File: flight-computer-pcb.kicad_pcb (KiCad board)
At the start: 4 copper layers, 140 x 80 mm, 3 parts, among them U1 Teensy4.1, U2 BMP390, U3 BNO055

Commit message: feat: add GND layer
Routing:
- added copper zone on In1.Cu, net GND
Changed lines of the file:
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@@
 		(layer "Edge.Cuts")
+	)
+	(zone
+		(net 4)
+		(net_name "GND")
+		(layer "In1.Cu")
+		(hatch edge 0.5)
+		(connect_pads
+			(clearance 0.5)
+		)
+		(min_thickness 0.25)
+		(filled_areas_thickness no)
+		(fill yes
+			(thermal_gap 0.5)
+			(thermal_bridge_width 0.5)
+		)
+		(polygon
+			(pts
+				(xy 71.177899 56) (xy 229.177899 56) (xy 229.177899 146) (xy 70.177899 146)
+			)
+		)
 	)
 	(embedded_fonts no)

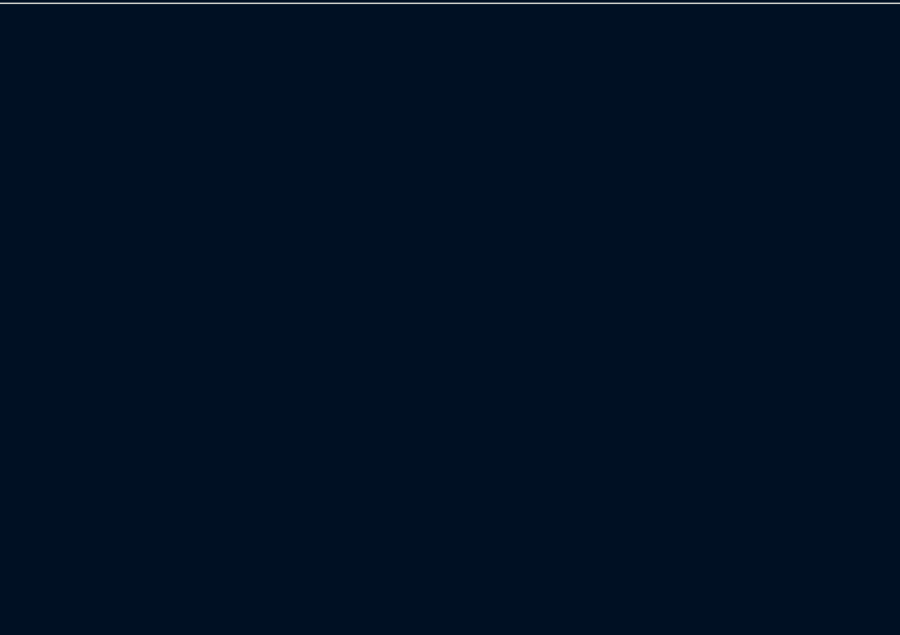
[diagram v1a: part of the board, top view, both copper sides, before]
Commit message: feat: add S13V10F5
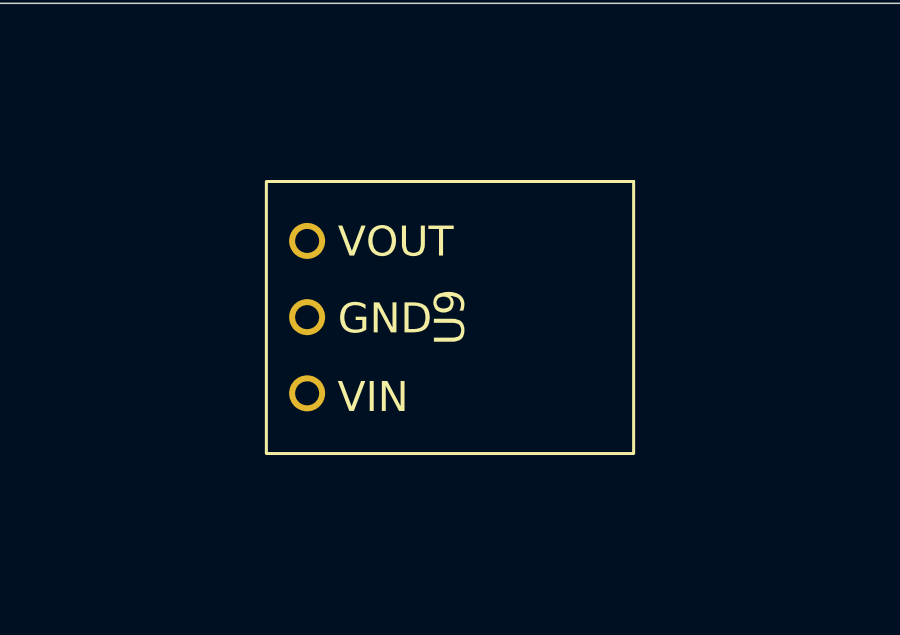
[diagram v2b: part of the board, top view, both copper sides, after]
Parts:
- added U9: S13V10F5, FlightComputer:S13V10F5, F.Cu at (199.8, 70.5)
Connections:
- U1 pad 20: unconnected-(U1-28_RX7-Pad20) -> /Parani_TX
- U1 pad 21: unconnected-(U1-29_TX7-Pad21) -> /Parani_RX
- U1 pad 22: unconnected-(U1-30_CRX3-Pad22) -> /Parani_CTS
